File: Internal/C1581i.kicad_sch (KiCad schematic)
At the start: 71 parts, among them CN1 FLOPPY POWER, CN2 FLOPPY, CN5 LEDS, CN7 INTERNAL IEC, CN8 EXTERNAL POWER, J1 PIN34, J2 PIN2, J3 DRIVE SELECT, J5 ROM SELECT, J90 Barrel_Jack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

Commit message: 1581i Update
Lots of re-routing to pack components tighter. PCB is now smaller. Added FPC connector to add Laptop PC drive support. Add board render.
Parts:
- removed J3: DRIVE SELECT, Connector_PinHeader_2.54mm:PinHeader_2x02_P2.54mm_Vertical, symbol Connector_Generic:Conn_02x02_Odd_Even
- added J3: PIN2, Connector_PinHeader_2.54mm:PinHeader_1x03_P2.54mm_Vertical, symbol Connector_Generic:Conn_01x03
- added J4: FPC, Connector_FFC-FPC:Molex_200528-0260_1x26-1MP_P1.00mm_Horizontal, symbol Connector_Generic:Conn_01x26
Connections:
- net DIRECTION: now also J4.12 (Pin_12)
- net GND: now also J3.2 (Pin_2), J4.15 (Pin_15), J4.17 (Pin_17), J4.23 (Pin_23), J4.25 (Pin_25)
- net INDEX: now also J4.2 (Pin_2)
- net MOTOREN: now also J4.10 (Pin_10)
- net READDATA: now also J4.24 (Pin_24)
- net SELECT0: now also J3.1 (Pin_1), J4.4 (Pin_4)
- net SELECT1: now also J3.3 (Pin_3)
- net SIDESELECT: now also J4.26 (Pin_26)
- net STEP: now also J4.14 (Pin_14)
- net TRACK00: now also J4.20 (Pin_20)
- net VCC: now also J4.1 (Pin_1), J4.3 (Pin_3), J4.5 (Pin_5)
- net WRITEDATA: now also J4.16 (Pin_16)
- net WRITEGATE: now also J4.18 (Pin_18)
- net WRITEPROTECT: now also J4.22 (Pin_22)
- net ~{DISKCHANGE}: now also J4.6 (Pin_6)
- net ~{RDY}: now also J4.8 (Pin_8)
- new net DENSITY: J4.9 (Pin_9)
- no-connect marks 24 -> 29
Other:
- note added: "C1581i DISK DRIVE (INTERNAL)"
- note added: "Laptop PC Drive Connector"
- note added: "UPDATED: 2024-02-08"
- note removed: "C1581 DISK DRIVE"
- note removed: "UPDATED: 2024-02-7"
- title: C1541 Disk Drive PCB with Enhancements -> C1581i Disk Drive PCB
- moved on the sheet: C1, C2, C3, C4, C90, C91, CN1, CN2, CN8, FB1, FB2, J1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

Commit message: Add Enable/Disable Jumper
Allows use of an external switch to enable/disable the drive.
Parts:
- added J6: DRIVE ENABLE, Connector_PinHeader_2.54mm:PinHeader_1x02_P2.54mm_Vertical, symbol Connector_Generic:Conn_01x02
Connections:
- net ~{ATN}: now also J6.2 (Pin_2); no longer EM2.1
- new net: EM2.1, J6.1 (Pin_1)
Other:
- note added: "UPDATED: 2024-02-11"
- note removed: "UPDATED: 2024-02-08"
- moved on the sheet: CN7, EM1, EM2, RP11D

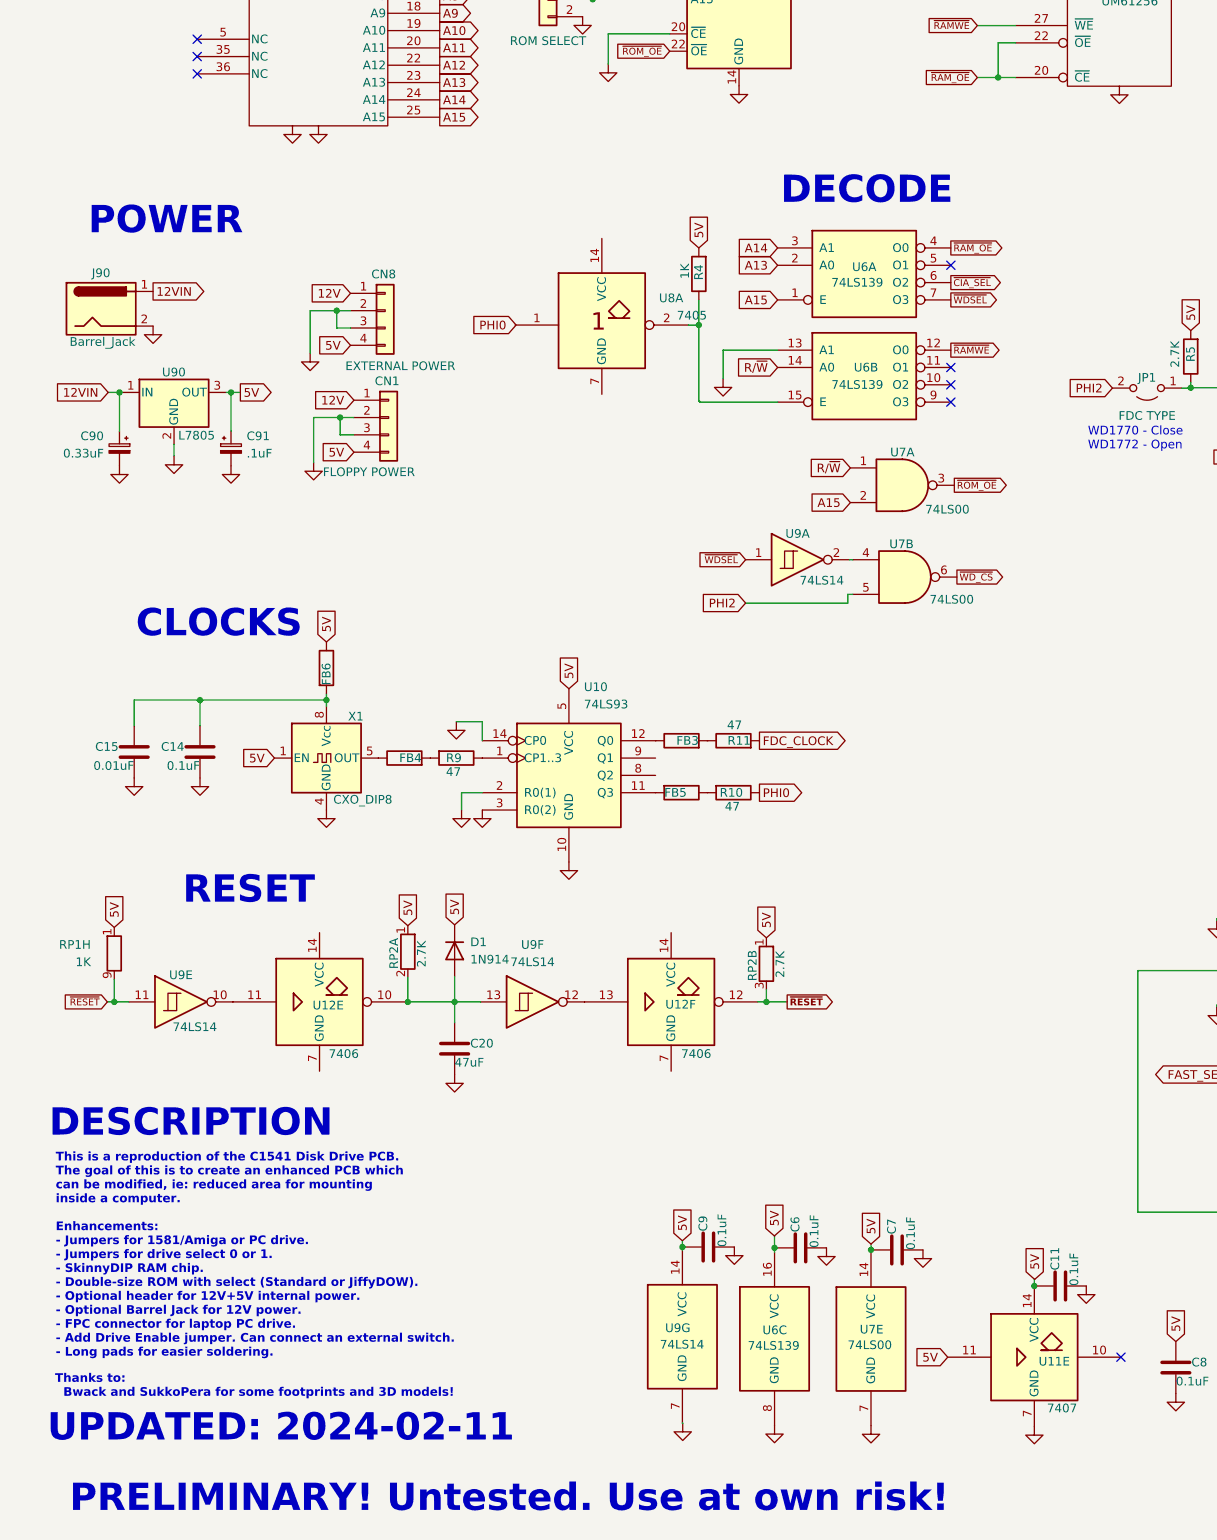
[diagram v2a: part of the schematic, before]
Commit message: 1581i - Fix 12v power
Fix 12V from barrel jack not connecting to floppy power. I am making  a small run of boards from JLCPCB to test the design.
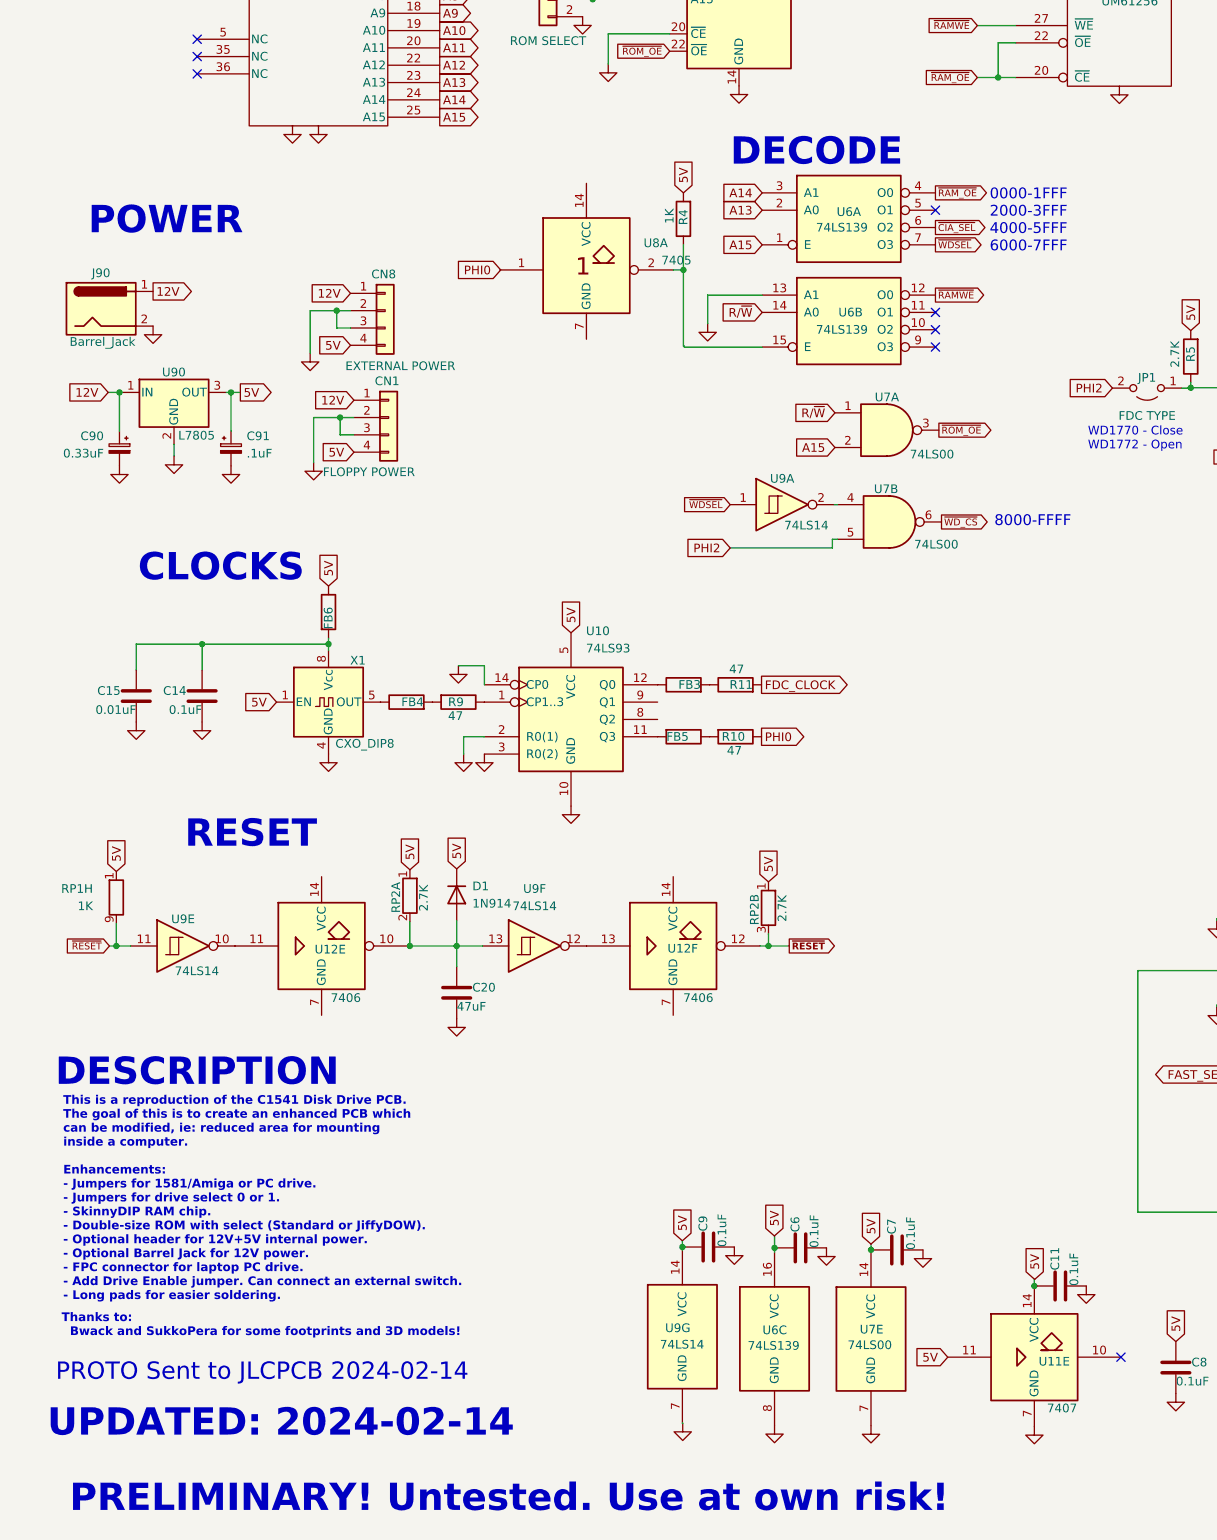
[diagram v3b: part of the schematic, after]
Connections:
- net 12VIN is gone; now on net 12V: C90.1, J90.1, U90.1 (IN)
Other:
- note added: "0000-1FFF 2000-3FFF 4000-5FFF 6000-7FFF"
- note added: "8000-FFFF"
- note added: "PROTO Sent to JLCPCB 2024-02-14"
- note added: "UPDATED: 2024-02-14"
- note removed: "UPDATED: 2024-02-11"
- moved on the sheet: C14, C15, C20, D1, FB3, FB4, FB5, FB6, R10, R11, R4, R9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
